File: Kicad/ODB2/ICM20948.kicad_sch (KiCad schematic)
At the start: 0 parts

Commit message: edit titles
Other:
- company: (none) -> GAUL
- title: (none) -> Acc/Gyro/Mag
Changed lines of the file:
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@@
 	(generator_version "8.0")
 	(paper "A4")
+	(title_block
+		(title "Acc/Gyro/Mag")
+		(date "2024-11-09")
+		(company "GAUL")
+	)
 )

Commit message: add titles
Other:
- note added: "Acce/Gyro/Mag"
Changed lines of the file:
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@@
 		(company "GAUL")
 	)
+	(text "Acce/Gyro/Mag"
+		(exclude_from_sim no)
+		(at 49.022 18.542 0)
+		(effects
+			(font
+				(size 6 6)
+				(thickness 1.2)
+				(bold yes)
+			)
+		)
+	)
 )

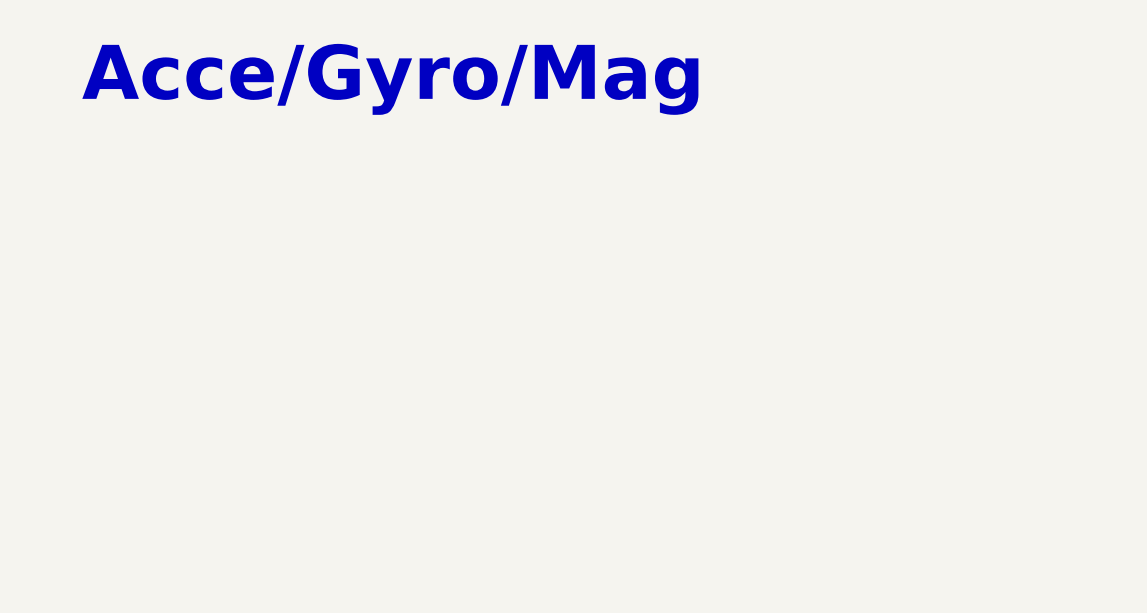
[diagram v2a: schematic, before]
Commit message: add sensors
ICM
L76L
MS580
PowerSupply
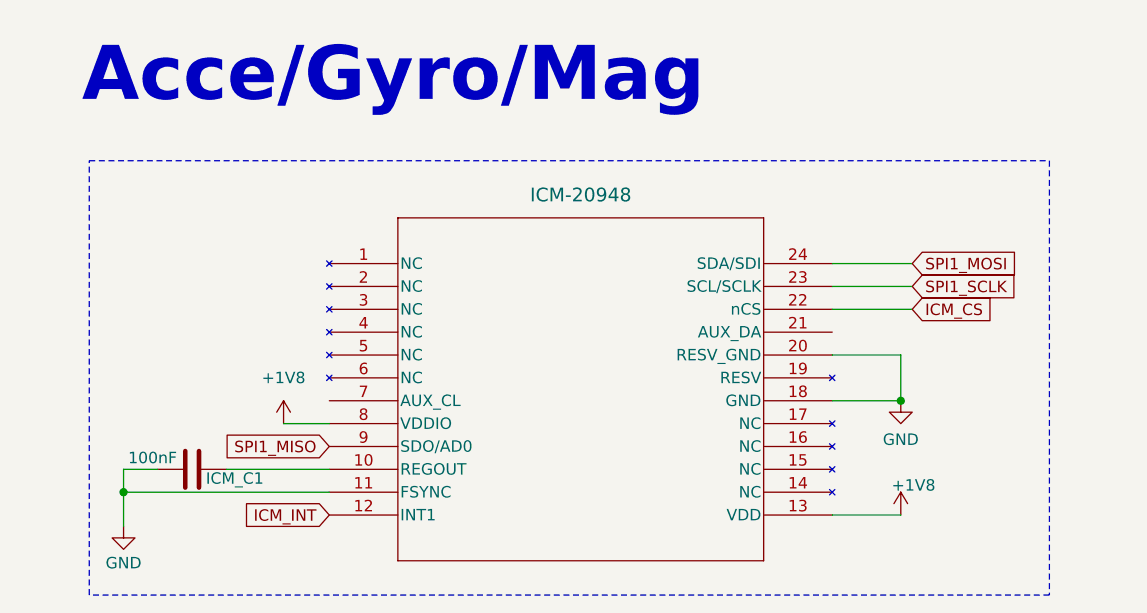
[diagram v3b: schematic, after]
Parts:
- added ICM_C1: 100nF, symbol Device:C
- added U6: ICM-20948, QFN24_3X3X0P9_IVS, symbol ODB_Lib:ICM-20948
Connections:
- new net: ICM_C1.1, U6.10 (REGOUT)
- new net +1V8: U6.13 (VDD), U6.8 (VDDIO)
- new net GND: ICM_C1.2, U6.11 (FSYNC), U6.18 (GND), U6.20 (RESV_GND)
- new net ICM_CS: U6.22 (nCS)
- new net ICM_INT: U6.12 (INT1)
- new net SPI1_MISO: U6.9 (SDO/AD0)
- new net SPI1_MOSI: U6.24 (SDA/SDI)
- new net SPI1_SCLK: U6.23 (SCL/SCLK)

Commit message: fix spi icm pinout
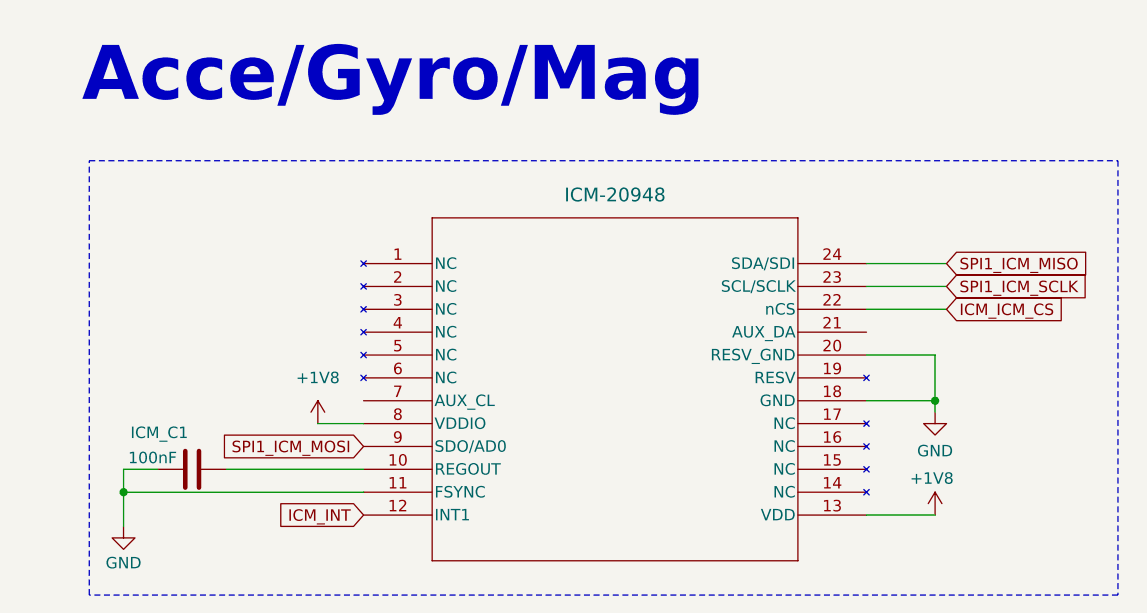
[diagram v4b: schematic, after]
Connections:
- net ICM_CS renamed ICM_ICM_CS
- net SPI1_MISO renamed SPI1_ICM_MOSI
- net SPI1_MOSI renamed SPI1_ICM_MISO
- net SPI1_SCLK renamed SPI1_ICM_SCLK
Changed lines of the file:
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@@
 	)
 	(junction
-		(at 105.41 54.61)
+		(at 109.22 54.61)
 		(diameter 0)
 		(color 0 0 0 0)
@@
 	(wire
 		(pts
-			(xy 36.83 57.15) (xy 41.91 57.15)
-		)
-		(stroke
-			(width 0)
-			(type default)
-		)
-	)
-	(wire
-		(pts
-			(xy 97.79 49.53) (xy 105.41 49.53)
-		)
-		(stroke
-			(width 0)
-			(type default)
-		)
-	)
-	(wire
-		(pts
-			(xy 97.79 54.61) (xy 105.41 54.61)
-		)
-		(stroke
-			(width 0)
-			(type default)
-		)
-	)
-	(wire
-		(pts
-			(xy 97.79 44.45) (xy 106.68 44.45)
+			(xy 40.64 57.15) (xy 45.72 57.15)
+		)
+		(stroke
+			(width 0)
+			(type default)
+		)
+	)
+	(wire
+		(pts
+			(xy 101.6 49.53) (xy 109.22 49.53)
+		)
+		(stroke
+			(width 0)
+			(type default)
+		)
+	)
+	(wire
+		(pts
+			(xy 109.22 55.88) (xy 109.22 54.61)
+		)
+		(stroke
+			(width 0)
+			(type default)
+		)
+	)
+	(wire
+		(pts
+			(xy 101.6 54.61) (xy 109.22 54.61)
+		)
+		(stroke
+			(width 0)
+			(type default)
+		)
+	)
+	(wire
+		(pts
+			(xy 101.6 44.45) (xy 110.49 44.45)
 		)
 		(stroke
@@
 	(wire
 		(pts
-			(xy 41.91 64.77) (xy 19.05 64.77)
+			(xy 45.72 64.77) (xy 19.05 64.77)
 		)
 		(stroke
@@
 	(wire
 		(pts
-			(xy 105.41 49.53) (xy 105.41 54.61)
-		)
-		(stroke
-			(width 0)
-			(type default)
-		)
-	)
-	(wire
-		(pts
-			(xy 30.48 62.23) (xy 41.91 62.23)
-		)
-		(stroke
-			(width 0)
-			(type default)
-		)
-	)
-	(wire
-		(pts
-			(xy 97.79 67.31) (xy 105.41 67.31)
-		)
-		(stroke
-			(width 0)
-			(type default)
-		)
-	)
-	(wire
-		(pts
-			(xy 97.79 39.37) (xy 106.68 39.37)
+			(xy 109.22 49.53) (xy 109.22 54.61)
+		)
+		(stroke
+			(width 0)
+			(type default)
+		)
+	)
+	(wire
+		(pts
+			(xy 30.48 62.23) (xy 45.72 62.23)
+		)
+		(stroke
+			(width 0)
+			(type default)
+		)
+	)
+	(wire
+		(pts
+			(xy 101.6 67.31) (xy 109.22 67.31)
+		)
+		(stroke
+			(width 0)
+			(type default)
+		)
+	)
+	(wire
+		(pts
+			(xy 101.6 39.37) (xy 110.49 39.37)
 		)
 		(stroke
@@
 	(wire
 		(pts
-			(xy 97.79 41.91) (xy 106.68 41.91)
+			(xy 101.6 41.91) (xy 110.49 41.91)
 		)
 		(stroke
@@
 	(rectangle
 		(start 15.24 27.94)
-		(end 121.92 76.2)
+		(end 129.54 76.2)
 		(stroke
 			(width 0)
@@
 		)
 	)
-	(global_label "SPI1_MOSI"
+	(global_label "SPI1_ICM_MISO"
 		(shape input)
-		(at 106.68 39.37 0)
+		(at 110.49 39.37 0)
 		(fields_autoplaced yes)
 		(effects
@@
 		)
 		(property "Intersheetrefs" "${INTERSHEET_REFS}"
-			(at 119.5228 39.37 0)
+			(at 127.6266 39.37 0)
 			(effects
 				(font
@@
 	(global_label "ICM_INT"
 		(shape input)
-		(at 41.91 67.31 180)
+		(at 45.72 67.31 180)
 		(fields_autoplaced yes)
 		(effects
@@
 		)
 		(property "Intersheetrefs" "${INTERSHEET_REFS}"
-			(at 31.7281 67.31 0)
+			(at 35.5381 67.31 0)
 			(effects
 				(font
@@
 		)
 	)
-	(global_label "ICM_CS"
+	(global_label "ICM_ICM_CS"
 		(shape input)
-		(at 106.68 44.45 0)
+		(at 110.49 44.45 0)
 		(fields_autoplaced yes)
 		(effects
@@
 		)
 		(property "Intersheetrefs" "${INTERSHEET_REFS}"
-			(at 116.4385 44.45 0)
+			(at 124.5423 44.45 0)
 			(effects
 				(font
@@
 		)
 	)
-	(global_label "SPI1_SCLK"
+	(global_label "SPI1_ICM_SCLK"
 		(shape input)
-		(at 106.68 41.91 0)
+		(at 110.49 41.91 0)
 		(fields_autoplaced yes)
 		(effects
@@
 		)
 		(property "Intersheetrefs" "${INTERSHEET_REFS}"
-			(at 119.7042 41.91 0)
+			(at 127.808 41.91 0)
 			(effects
 				(font
@@
 		)
 	)
-	(global_label "SPI1_MISO"
+	(global_label "SPI1_ICM_MOSI"
 		(shape input)
-		(at 41.91 59.69 180)
+		(at 45.72 59.69 180)
 		(fields_autoplaced yes)
 		(effects
@@
 		)
 		(property "Intersheetrefs" "${INTERSHEET_REFS}"
-			(at 29.0672 59.69 0)
+			(at 28.5834 59.69 0)
 			(effects
 				(font
@@
 	(symbol
 		(lib_id "power:+3V3")
-		(at 105.41 67.31 0)
+		(at 109.22 67.31 0)
 		(unit 1)
 		(exclude_from_sim no)
@@
 		(dnp no)
 		(property "Reference" "#PWR056"
-			(at 105.41 71.12 0)
+			(at 109.22 71.12 0)
 			(effects
 				(font
@@
 		)
 		(property "Value" "+1V8"
-			(at 104.394 64.008 0)
+			(at 106.426 63.246 0)
 			(effects
 				(font
@@
 		)
 		(property "Footprint" ""
-			(at 105.41 67.31 0)
+			(at 109.22 67.31 0)
 			(effects
 				(font
@@
 		)
 		(property "Datasheet" ""
-			(at 105.41 67.31 0)
+			(at 109.22 67.31 0)
 			(effects
 				(font
@@
 		)
 		(property "Description" "Power symbol creates a global label with name \"+3V3\""
-			(at 105.41 67.31 0)
+			(at 109.22 67.31 0)
 			(effects
 				(font
@@
 		(dnp no)
 		(property "Reference" "ICM_C1"
-			(at 28.194 63.246 90)
+			(at 19.812 58.166 90)
 			(effects
 				(font
@@
 	(symbol
 		(lib_id "ODB_Lib:ICM-20948")
-		(at 41.91 39.37 0)
+		(at 45.72 39.37 0)
 		(unit 1)
 		(exclude_from_sim no)
@@
 		(fields_autoplaced yes)
 		(property "Reference" "U6"
-			(at 70.866 45.212 0)
+			(at 74.676 45.212 0)
 			(effects
 				(font
@@
 		)
 		(property "Value" "ICM-20948"
-			(at 69.85 31.75 0)
+			(at 73.66 31.75 0)
 			(effects
 				(font
@@
 		)
 		(property "Footprint" "QFN24_3X3X0P9_IVS"
-			(at 69.342 39.878 0)
+			(at 73.152 39.878 0)
 			(effects
 				(font
@@
 		)
 		(property "Datasheet" "ICM-20948"
-			(at 70.866 42.418 0)
+			(at 74.676 42.418 0)
 			(effects
 				(font
@@
 		)
 		(property "Description" ""
-			(at 41.91 39.37 0)
+			(at 45.72 39.37 0)
 			(effects
 				(font
@@
 	(symbol
 		(lib_id "power:+1V8")
-		(at 36.83 57.15 0)
+		(at 40.64 57.15 0)
 		(unit 1)
 		(exclude_from_sim no)
@@
 		(fields_autoplaced yes)
 		(property "Reference" "#PWR054"
-			(at 36.83 60.96 0)
+			(at 40.64 60.96 0)
 			(effects
 				(font
@@
 		)
 		(property "Value" "+1V8"
-			(at 36.83 52.07 0)
+			(at 40.64 52.07 0)
 			(effects
 				(font
@@
 		)
 		(property "Footprint" ""
-			(at 36.83 57.15 0)
+			(at 40.64 57.15 0)
 			(effects
 				(font
@@
 		)
 		(property "Datasheet" ""
-			(at 36.83 57.15 0)
+			(at 40.64 57.15 0)
 			(effects
 				(font
@@
 		)
 		(property "Description" "Power symbol creates a global label with name \"+1V8\""
-			(at 36.83 57.15 0)
+			(at 40.64 57.15 0)
 			(effects
 				(font
@@
 	(symbol
 		(lib_id "power:GND")
-		(at 105.41 54.61 0)
+		(at 109.22 55.88 0)
 		(unit 1)
 		(exclude_from_sim no)
@@
 		(dnp no)
 		(property "Reference" "#PWR055"
-			(at 105.41 60.96 0)
+			(at 109.22 62.23 0)
 			(effects
 				(font
@@
 		)
 		(property "Value" "GND"
-			(at 105.41 58.928 0)
+			(at 109.22 60.198 0)
 			(effects
 				(font
@@
 		)
 		(property "Footprint" ""
-			(at 105.41 54.61 0)
+			(at 109.22 55.88 0)
 			(effects
 				(font
@@
 		)
 		(property "Datasheet" ""
-			(at 105.41 54.61 0)
+			(at 109.22 55.88 0)
 			(effects
 				(font
@@
 		)
 		(property "Description" "Power symbol creates a global label with name \"GND\" , ground"
-			(at 105.41 54.61 0)
-			(effects
-				(font
+			(at 109.22 55.88 0)
+			(effects
+				(font
